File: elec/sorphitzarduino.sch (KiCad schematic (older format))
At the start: 13 parts, among them J1 9V_BATT, J2 SWITCH, J3 AUDIO_JACK, U1 ARDUINO_MICRO_SHIELD

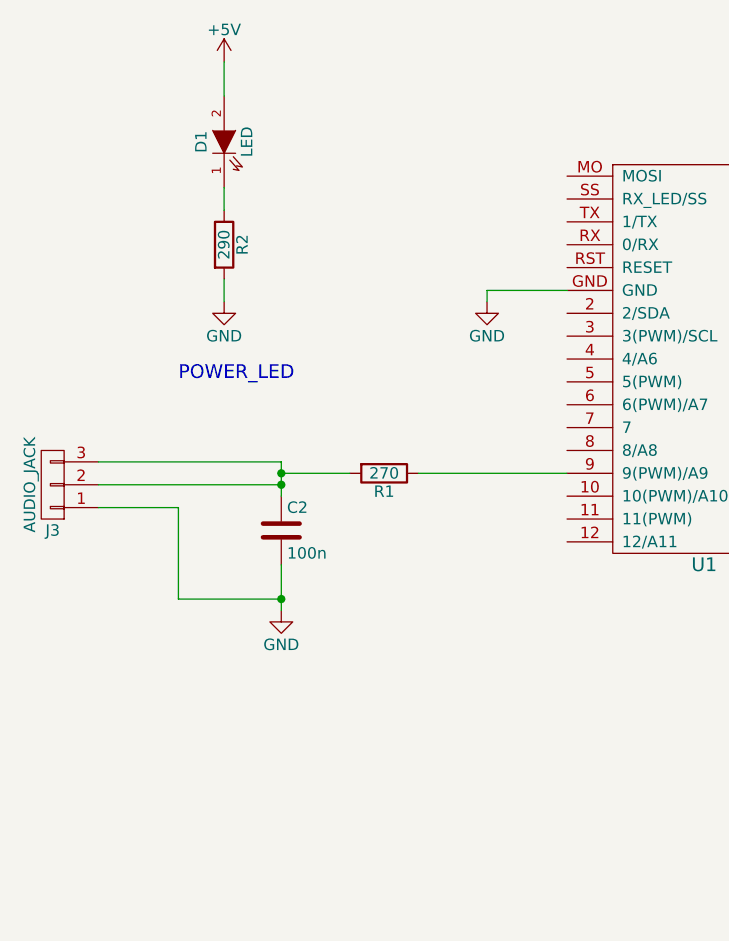
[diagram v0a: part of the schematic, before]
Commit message: Upating to HIFI output circuit, and adding sontrol of LED
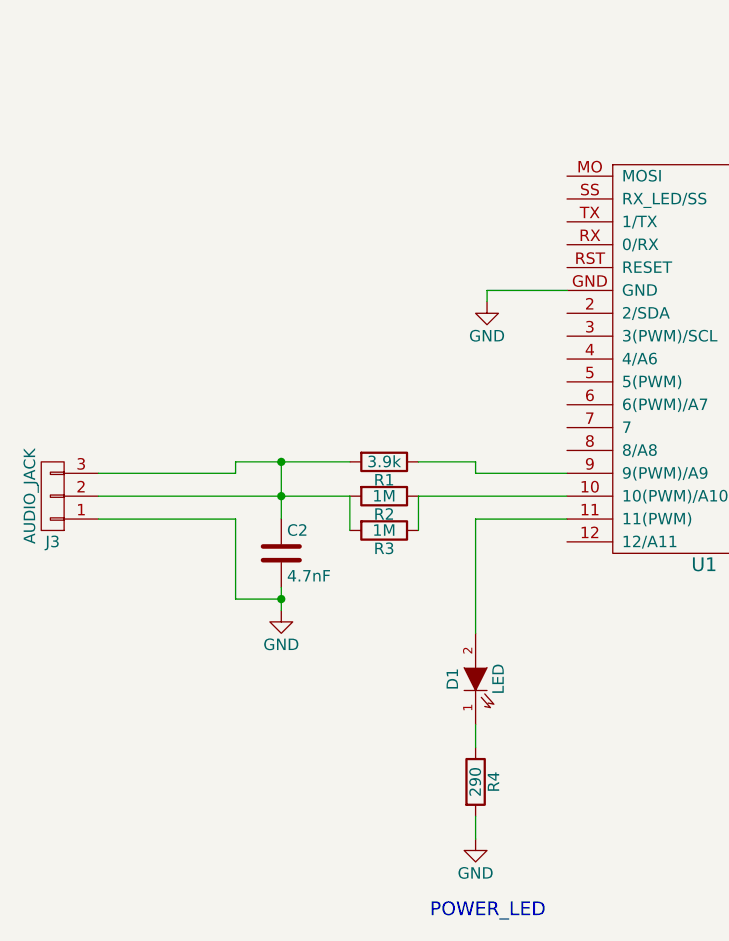
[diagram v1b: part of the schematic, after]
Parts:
- added R2, R3: 1M, Resistors_ThroughHole:Resistor_Horizontal_RM10mm, symbol R
- C2: value 100n -> 4.7nF
- R1: value 270 -> 3.9k
- renumbered R2 to R4
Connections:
- net +5V: no longer D1.2 (A)
- net at U1.10 (10(PWM)/A10): now also R2.1, R3.1
- net at U1.11 (11(PWM)): now also D1.2 (A)
- net at C2.1, J3.2 (P2), J3.3 (P3)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: now also R2.2, R3.2
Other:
- moved on the sheet: C2, D1, J3, R1, R4
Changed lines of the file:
@@
 Connection ~ 7250 3250
-$Comp
-L R R1
-U 1 1 5BFA081C
-P 4500 4250
-F 0 "R1" V 4580 4250 50  0000 C CNN
-F 1 "270" V 4500 4250 50  0000 C CNN
-F 2 "Resistors_ThroughHole:Resistor_Horizontal_RM10mm" V 4430 4250 50  0001 C CNN
-F 3 "" H 4500 4250 50  0000 C CNN
-	1    4500 4250
-	0    1    1    0
-$EndComp
 $Comp
 L C C2
 U 1 1 5BFA0990
-P 4050 4500
-F 0 "C2" H 4075 4600 50  0000 L CNN
-F 1 "100n" H 4075 4400 50  0000 L CNN
-F 2 "Capacitors_ThroughHole:C_Disc_D6_P5" H 4088 4350 50  0001 C CNN
-F 3 "" H 4050 4500 50  0000 C CNN
-	1    4050 4500
+P 4050 4600
+F 0 "C2" H 4075 4700 50  0000 L CNN
+F 1 "4.7nF" H 4075 4500 50  0000 L CNN
+F 2 "Capacitors_ThroughHole:C_Disc_D6_P5" H 4088 4450 50  0001 C CNN
+F 3 "" H 4050 4600 50  0000 C CNN
+	1    4050 4600
 	1    0    0    -1
 $EndComp
@@
 	1    0    0    -1
 $EndComp
-Wire Wire Line
-	4050 4650 4050 4850
-Wire Wire Line
-	4350 4250 4050 4250
-Wire Wire Line
-	4050 4200 4050 4350
-Wire Wire Line
-	4650 4250 5300 4250
 $Comp
 L CONN_01X03 J3
 U 1 1 5BFA0BF7
-P 3050 4300
-F 0 "J3" H 3050 4500 50  0000 C CNN
-F 1 "AUDIO_JACK" V 3150 4300 50  0000 C CNN
-F 2 "Pin_Headers:Pin_Header_Straight_1x03" H 3050 4300 50  0001 C CNN
-F 3 "" H 3050 4300 50  0000 C CNN
-	1    3050 4300
+P 3050 4350
+F 0 "J3" H 3050 4550 50  0000 C CNN
+F 1 "AUDIO_JACK" V 3150 4350 50  0000 C CNN
+F 2 "Pin_Headers:Pin_Header_Straight_1x03" H 3050 4350 50  0001 C CNN
+F 3 "" H 3050 4350 50  0000 C CNN
+	1    3050 4350
 	-1   0    0    1
 $EndComp
 Wire Wire Line
-	3250 4200 4050 4200
-Connection ~ 4050 4250
-Wire Wire Line
-	4050 4300 3250 4300
-Connection ~ 4050 4300
-Wire Wire Line
-	3250 4400 3600 4400
-Wire Wire Line
-	3600 4400 3600 4800
-Wire Wire Line
-	3600 4800 4050 4800
+	3850 4200 4350 4200
+Wire Wire Line
+	3250 4450 3850 4450
+Wire Wire Line
+	3850 4450 3850 4800
+Wire Wire Line
+	3850 4800 4050 4800
 Connection ~ 4050 4800
 $Comp
 L LED D1
 U 1 1 5BFA0F30
-P 3800 2800
-F 0 "D1" H 3800 2900 50  0000 C CNN
-F 1 "LED" H 3800 2700 50  0000 C CNN
-F 2 "LEDs:LED-5MM" H 3800 2800 50  0001 C CNN
-F 3 "" H 3800 2800 50  0000 C CNN
-	1    3800 2800
+P 4900 5150
+F 0 "D1" H 4900 5250 50  0000 C CNN
+F 1 "LED" H 4900 5050 50  0000 C CNN
+F 2 "LEDs:LED-5MM" H 4900 5150 50  0001 C CNN
+F 3 "" H 4900 5150 50  0000 C CNN
+	1    4900 5150
 	0    -1   -1   0
 $EndComp
 $Comp
-L +5V #PWR06
-U 1 1 5BFA10BA
-P 3800 2450
-F 0 "#PWR06" H 3800 2300 50  0001 C CNN
-F 1 "+5V" H 3800 2590 50  0000 C CNN
-F 2 "" H 3800 2450 50  0000 C CNN
-F 3 "" H 3800 2450 50  0000 C CNN
-	1    3800 2450
-	1    0    0    -1
-$EndComp
-$Comp
-L GND #PWR07
+L GND #PWR06
 U 1 1 5BFA10FE
-P 3800 3500
-F 0 "#PWR07" H 3800 3250 50  0001 C CNN
-F 1 "GND" H 3800 3350 50  0000 C CNN
-F 2 "" H 3800 3500 50  0000 C CNN
-F 3 "" H 3800 3500 50  0000 C CNN
-	1    3800 3500
-	1    0    0    -1
-$EndComp
-$Comp
-L R R2
+P 4900 5850
+F 0 "#PWR06" H 4900 5600 50  0001 C CNN
+F 1 "GND" H 4900 5700 50  0000 C CNN
+F 2 "" H 4900 5850 50  0000 C CNN
+F 3 "" H 4900 5850 50  0000 C CNN
+	1    4900 5850
+	1    0    0    -1
+$EndComp
+$Comp
+L R R4
 U 1 1 5BFA11AE
-P 3800 3250
-F 0 "R2" V 3880 3250 50  0000 C CNN
-F 1 "290" V 3800 3250 50  0000 C CNN
-F 2 "Resistors_ThroughHole:Resistor_Horizontal_RM10mm" V 3730 3250 50  0001 C CNN
-F 3 "" H 3800 3250 50  0000 C CNN
-	1    3800 3250
-	1    0    0    -1
-$EndComp
-Wire Wire Line
-	3800 2450 3800 2600
-Wire Wire Line
-	3800 3000 3800 3100
-Wire Wire Line
-	3800 3400 3800 3500
-Text Notes 3600 3850 0    60   ~ 0
+P 4900 5600
+F 0 "R4" V 4980 5600 50  0000 C CNN
+F 1 "290" V 4900 5600 50  0000 C CNN
+F 2 "Resistors_ThroughHole:Resistor_Horizontal_RM10mm" V 4830 5600 50  0001 C CNN
+F 3 "" H 4900 5600 50  0000 C CNN
+	1    4900 5600
+	1    0    0    -1
+$EndComp
+Wire Wire Line
+	4900 5350 4900 5450
+Wire Wire Line
+	4900 5750 4900 5850
+Text Notes 4700 6200 0    60   ~ 0
 POWER_LED
 $Comp
@@
 Connection ~ 7500 4900
 $Comp
-L GND #PWR08
+L GND #PWR07
 U 1 1 5BFA60DB
 P 4950 3500
-F 0 "#PWR08" H 4950 3250 50  0001 C CNN
+F 0 "#PWR07" H 4950 3250 50  0001 C CNN
 F 1 "GND" H 4950 3350 50  0000 C CNN
 F 2 "" H 4950 3500 50  0000 C CNN
@@
 Wire Wire Line
 	4950 3450 4950 3500
+Wire Wire Line
+	5300 4450 4900 4450
+Wire Wire Line
+	4900 4450 4900 4950
+$Comp
+L R R1
+U 1 1 5BFA081C
+P 4500 4200
+F 0 "R1" V 4580 4200 50  0000 C CNN
+F 1 "3.9k" V 4500 4200 50  0000 C CNN
+F 2 "Resistors_ThroughHole:Resistor_Horizontal_RM10mm" V 4430 4200 50  0001 C CNN
+F 3 "" H 4500 4200 50  0000 C CNN
+	1    4500 4200
+	0    1    1    0
+$EndComp
+$Comp
+L R R2
+U 1 1 5C037AD8
+P 4500 4350
+F 0 "R2" V 4580 4350 50  0000 C CNN
+F 1 "1M" V 4500 4350 50  0000 C CNN
+F 2 "Resistors_ThroughHole:Resistor_Horizontal_RM10mm" V 4430 4350 50  0001 C CNN
+F 3 "" H 4500 4350 50  0000 C CNN
+	1    4500 4350
+	0    1    1    0
+$EndComp
+$Comp
+L R R3
+U 1 1 5C037B46
+P 4500 4500
+F 0 "R3" V 4580 4500 50  0000 C CNN
+F 1 "1M" V 4500 4500 50  0000 C CNN
+F 2 "Resistors_ThroughHole:Resistor_Horizontal_RM10mm" V 4430 4500 50  0001 C CNN
+F 3 "" H 4500 4500 50  0000 C CNN
+	1    4500 4500
+	0    1    1    0
+$EndComp
+Wire Wire Line
+	5300 4350 4650 4350
+Wire Wire Line
+	4650 4350 4650 4500
+Wire Wire Line
+	4050 4200 4050 4450
+Wire Wire Line
+	4050 4750 4050 4850
+Wire Wire Line
+	3250 4350 4350 4350
+Wire Wire Line
+	4350 4350 4350 4500
+Wire Wire Line
+	4650 4200 4900 4200
+Wire Wire Line
+	4900 4200 4900 4250
+Wire Wire Line
+	4900 4250 5300 4250
+Connection ~ 4050 4200
+Connection ~ 4050 4350
+Wire Wire Line
+	3250 4250 3850 4250
+Wire Wire Line
+	3850 4250 3850 4200
 $EndSCHEMATC

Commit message: Initial attempts at exporting png files for cutting
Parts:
- C1: symbol CP -> Bourne_PTA6043:CP
- C2: symbol C -> Bourne_PTA6043:C
- D1: symbol LED -> Bourne_PTA6043:LED
- J1, J2: symbol CONN_01X02 -> sorphitzarduino-rescue:CONN_01X02
- J3: symbol CONN_01X03 -> sorphitzarduino-rescue:CONN_01X03
- R1, R2, R3, R4: symbol R -> Bourne_PTA6043:R
- RV1, RV2, RV3, RV4: symbol Bourne_Slider -> Bourne_PTA6043:Bourne_Slider
- U1: symbol ARDUINO_MICRO_SHIELD -> sorphitzarduino-rescue:ARDUINO_MICRO_SHIELD
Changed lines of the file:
@@
-EESchema Schematic File Version 2
-LIBS:power
-LIBS:device
-LIBS:transistors
-LIBS:conn
-LIBS:linear
-LIBS:regul
-LIBS:74xx
-LIBS:cmos4000
-LIBS:adc-dac
-LIBS:memory
-LIBS:xilinx
-LIBS:microcontrollers
-LIBS:dsp
-LIBS:microchip
-LIBS:analog_switches
-LIBS:motorola
-LIBS:texas
-LIBS:intel
-LIBS:audio
-LIBS:interface
-LIBS:digital-audio
-LIBS:philips
-LIBS:display
-LIBS:cypress
-LIBS:siliconi
-LIBS:opto
-LIBS:atmel
-LIBS:contrib
-LIBS:valves
-LIBS:arduino_micro_shield
-LIBS:Bourne_PTA6043
+EESchema Schematic File Version 4
 LIBS:sorphitzarduino-cache
-EELAYER 25 0
+EELAYER 26 0
 EELAYER END
 $Descr A4 11693 8268
@@
 $EndDescr
 $Comp
-L GND #PWR01
+L power:GND #PWR01
 U 1 1 5BF9F106
 P 7100 4950
@@
 $EndComp
 $Comp
-L ARDUINO_MICRO_SHIELD U1
+L sorphitzarduino-rescue:ARDUINO_MICRO_SHIELD U1
 U 1 1 5BF9F1BE
 P 5500 2900
@@
 $EndComp
 $Comp
-L CONN_01X02 J1
+L sorphitzarduino-rescue:CONN_01X02 J1
 U 1 1 5BF9F43C
 P 8150 3200
@@
 $EndComp
 $Comp
-L GND #PWR02
+L power:GND #PWR02
 U 1 1 5BF9F4FC
 P 7100 3350
@@
 $EndComp
 $Comp
-L +5V #PWR03
+L power:+5V #PWR03
 U 1 1 5BF9F94F
 P 6850 4800
@@
 $EndComp
 $Comp
-L +5V #PWR04
+L power:+5V #PWR04
 U 1 1 5BF9F98F
 P 6850 3450
@@
 	7950 3150 7550 3150
 Wire Wire Line
-	7050 2800 7400 2800
-Wire Wire Line
-	6650 3250 7950 3250
+	7050 2800 7250 2800
+Wire Wire Line
+	6650 3250 7100 3250
 Wire Wire Line
 	7100 3350 7100 3250
@@
 	6850 4800 7050 4800
 $Comp
-L CONN_01X02 J2
+L sorphitzarduino-rescue:CONN_01X02 J2
 U 1 1 5BF9FCCD
 P 8150 2550
@@
 Wire Wire Line
 	7550 2600 7550 3150
-Connection ~ 7550 3150
 Wire Wire Line
 	7950 2500 7400 2500
 Wire Wire Line
 	7400 2500 7400 2800
-Connection ~ 7400 2800
-Wire Wire Line
-	7050 4350 7050 4900
+Wire Wire Line
+	7050 4350 7050 4800
 Wire Wire Line
 	7050 4350 6650 4350
@@
 	7050 3150 6650 3150
 $Comp
-L CP C1
+L Bourne_PTA6043:CP C1
 U 1 1 5BFA0508
 P 7250 3000
@@
 Connection ~ 7250 3250
 $Comp
-L C C2
+L Bourne_PTA6043:C C2
 U 1 1 5BFA0990
 P 4050 4600
@@
 $EndComp
 $Comp
-L GND #PWR05
+L power:GND #PWR05
 U 1 1 5BFA09E9
 P 4050 4850
@@
 $EndComp
 $Comp
-L CONN_01X03 J3
+L sorphitzarduino-rescue:CONN_01X03 J3
 U 1 1 5BFA0BF7
 P 3050 4350
@@
 $EndComp
 Wire Wire Line
-	3850 4200 4350 4200
+	3850 4200 4050 4200
 Wire Wire Line
 	3250 4450 3850 4450
@@
 Connection ~ 4050 4800
 $Comp
-L LED D1
+L Bourne_PTA6043:LED D1
 U 1 1 5BFA0F30
 P 4900 5150
@@
 $EndComp
 $Comp
-L GND #PWR06
+L power:GND #PWR06
 U 1 1 5BFA10FE
 P 4900 5850
@@
 $EndComp
 $Comp
-L R R4
+L Bourne_PTA6043:R R4
 U 1 1 5BFA11AE
 P 4900 5600
@@
 POWER_LED
 $Comp
-L Bourne_Slider RV1
+L Bourne_PTA6043:Bourne_Slider RV1
 U 1 1 5BFA5669
 P 7750 4600
@@
 $EndComp
 $Comp
-L Bourne_Slider RV2
+L Bourne_PTA6043:Bourne_Slider RV2
 U 1 1 5BFA57ED
 P 8450 4600
@@
 $EndComp
 $Comp
-L Bourne_Slider RV3
+L Bourne_PTA6043:Bourne_Slider RV3
 U 1 1 5BFA5836
 P 9150 4600
@@
 $EndComp
 $Comp
-L Bourne_Slider RV4
+L Bourne_PTA6043:Bourne_Slider RV4
 U 1 1 5BFA58DD
 P 9850 4600
@@
 	9850 3950 6650 3950
 Wire Wire Line
-	7100 4950 10100 4950
+	7100 4950 8000 4950
 Wire Wire Line
 	10100 4950 10100 4600
@@
 Connection ~ 8000 4950
 Wire Wire Line
-	7050 4900 9600 4900
+	7050 4900 7500 4900
 Wire Wire Line
 	9600 4900 9600 4600
@@
 Connection ~ 7500 4900
 $Comp
-L GND #PWR07
+L power:GND #PWR07
 U 1 1 5BFA60DB
 P 4950 3500
@@
 	4900 4450 4900 4950
 $Comp
-L R R1
+L Bourne_PTA6043:R R1
 U 1 1 5BFA081C
 P 4500 4200
@@
 $EndComp
 $Comp
-L R R2
+L Bourne_PTA6043:R R2
 U 1 1 5C037AD8
 P 4500 4350
@@
 $EndComp
 $Comp
-L R R3
+L Bourne_PTA6043:R R3
 U 1 1 5C037B46
 P 4500 4500
@@
 	4650 4350 4650 4500
 Wire Wire Line
-	4050 4200 4050 4450
-Wire Wire Line
-	4050 4750 4050 4850
-Wire Wire Line
-	3250 4350 4350 4350
+	4050 4200 4050 4350
+Wire Wire Line
+	4050 4750 4050 4800
+Wire Wire Line
+	3250 4350 4050 4350
 Wire Wire Line
 	4350 4350 4350 4500
@@
 Wire Wire Line
 	3850 4250 3850 4200
+Wire Wire Line
+	7100 3250 7250 3250
+Wire Wire Line
+	7050 4800 7050 4900
+Wire Wire Line
+	7250 2800 7400 2800
+Wire Wire Line
+	7250 3250 7950 3250
+Wire Wire Line
+	4050 4800 4050 4850
+Wire Wire Line
+	9400 4950 10100 4950
+Wire Wire Line
+	8700 4950 9400 4950
+Wire Wire Line
+	8000 4950 8700 4950
+Wire Wire Line
+	8900 4900 9600 4900
+Wire Wire Line
+	8200 4900 8900 4900
+Wire Wire Line
+	7500 4900 8200 4900
+Wire Wire Line
+	4050 4200 4350 4200
+Wire Wire Line
+	4050 4350 4050 4450
+Wire Wire Line
+	4050 4350 4350 4350
 $EndSCHEMATC

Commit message: Generating better PNG files for milling
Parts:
- added J4, J? (x3): Mounting Hole, MountingHole:MountingHole_3.2mm_M3, symbol Connector_Generic:Conn_01x01
- C1: symbol Bourne_PTA6043:CP -> sorphitzarduino-rescue:CP-Bourne_PTA6043
- C2: symbol Bourne_PTA6043:C -> sorphitzarduino-rescue:C-Bourne_PTA6043
- D1: symbol Bourne_PTA6043:LED -> sorphitzarduino-rescue:LED-Bourne_PTA6043
- J1, J2: symbol sorphitzarduino-rescue:CONN_01X02 -> sorphitzarduino-rescue:CONN_01X02-sorphitzarduino-rescue
- J3: symbol sorphitzarduino-rescue:CONN_01X03 -> sorphitzarduino-rescue:CONN_01X03-sorphitzarduino-rescue
- R1, R2, R3, R4: symbol Bourne_PTA6043:R -> sorphitzarduino-rescue:R-Bourne_PTA6043
- RV1, RV2, RV3, RV4: symbol Bourne_PTA6043:Bourne_Slider -> sorphitzarduino-rescue:Bourne_Slider-Bourne_PTA6043
- U1: symbol sorphitzarduino-rescue:ARDUINO_MICRO_SHIELD -> sorphitzarduino-rescue:ARDUINO_MICRO_SHIELD-sorphitzarduino-rescue
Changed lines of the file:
@@
 $EndComp
 $Comp
-L sorphitzarduino-rescue:ARDUINO_MICRO_SHIELD U1
+L sorphitzarduino-rescue:ARDUINO_MICRO_SHIELD-sorphitzarduino-rescue U1
 U 1 1 5BF9F1BE
 P 5500 2900
@@
 $EndComp
 $Comp
-L sorphitzarduino-rescue:CONN_01X02 J1
+L sorphitzarduino-rescue:CONN_01X02-sorphitzarduino-rescue J1
 U 1 1 5BF9F43C
 P 8150 3200
@@
 	6850 4800 7050 4800
 $Comp
-L sorphitzarduino-rescue:CONN_01X02 J2
+L sorphitzarduino-rescue:CONN_01X02-sorphitzarduino-rescue J2
 U 1 1 5BF9FCCD
 P 8150 2550
@@
 	7050 3150 6650 3150
 $Comp
-L Bourne_PTA6043:CP C1
+L sorphitzarduino-rescue:CP-Bourne_PTA6043 C1
 U 1 1 5BFA0508
 P 7250 3000
@@
 Connection ~ 7250 3250
 $Comp
-L Bourne_PTA6043:C C2
+L sorphitzarduino-rescue:C-Bourne_PTA6043 C2
 U 1 1 5BFA0990
 P 4050 4600
@@
 $EndComp
 $Comp
-L sorphitzarduino-rescue:CONN_01X03 J3
+L sorphitzarduino-rescue:CONN_01X03-sorphitzarduino-rescue J3
 U 1 1 5BFA0BF7
 P 3050 4350
@@
 Connection ~ 4050 4800
 $Comp
-L Bourne_PTA6043:LED D1
+L sorphitzarduino-rescue:LED-Bourne_PTA6043 D1
 U 1 1 5BFA0F30
 P 4900 5150
@@
 $EndComp
 $Comp
-L Bourne_PTA6043:R R4
+L sorphitzarduino-rescue:R-Bourne_PTA6043 R4
 U 1 1 5BFA11AE
 P 4900 5600
@@
 POWER_LED
 $Comp
-L Bourne_PTA6043:Bourne_Slider RV1
+L sorphitzarduino-rescue:Bourne_Slider-Bourne_PTA6043 RV1
 U 1 1 5BFA5669
 P 7750 4600
@@
 $EndComp
 $Comp
-L Bourne_PTA6043:Bourne_Slider RV2
+L sorphitzarduino-rescue:Bourne_Slider-Bourne_PTA6043 RV2
 U 1 1 5BFA57ED
 P 8450 4600
@@
 $EndComp
 $Comp
-L Bourne_PTA6043:Bourne_Slider RV3
+L sorphitzarduino-rescue:Bourne_Slider-Bourne_PTA6043 RV3
 U 1 1 5BFA5836
 P 9150 4600
@@
 $EndComp
 $Comp
-L Bourne_PTA6043:Bourne_Slider RV4
+L sorphitzarduino-rescue:Bourne_Slider-Bourne_PTA6043 RV4
 U 1 1 5BFA58DD
 P 9850 4600
@@
 	4900 4450 4900 4950
 $Comp
-L Bourne_PTA6043:R R1
+L sorphitzarduino-rescue:R-Bourne_PTA6043 R1
 U 1 1 5BFA081C
 P 4500 4200
@@
 $EndComp
 $Comp
-L Bourne_PTA6043:R R2
+L sorphitzarduino-rescue:R-Bourne_PTA6043 R2
 U 1 1 5C037AD8
 P 4500 4350
@@
 $EndComp
 $Comp
-L Bourne_PTA6043:R R3
+L sorphitzarduino-rescue:R-Bourne_PTA6043 R3
 U 1 1 5C037B46
 P 4500 4500
@@
 Wire Wire Line
 	4050 4350 4350 4350
+$Comp
+L Connector_Generic:Conn_01x01 J4
+U 1 1 5C079185
+P 3000 2000
+F 0 "J4" H 3079 2042 50  0000 L CNN
+F 1 "Mounting Hole" H 3079 1951 50  0000 L CNN
+F 2 "MountingHole:MountingHole_3.2mm_M3" H 3000 2000 50  0001 C CNN
+F 3 "~" H 3000 2000 50  0001 C CNN
+	1    3000 2000
+	1    0    0    -1
+$EndComp
+$Comp
+L Connector_Generic:Conn_01x01 J?
+U 1 1 5C07ACAF
+P 3000 2250
+F 0 "J?" H 3079 2292 50  0000 L CNN
+F 1 "Mounting Hole" H 3079 2201 50  0000 L CNN
+F 2 "MountingHole:MountingHole_3.2mm_M3" H 3000 2250 50  0001 C CNN
+F 3 "~" H 3000 2250 50  0001 C CNN
+	1    3000 2250
+	1    0    0    -1
+$EndComp
+$Comp
+L Connector_Generic:Conn_01x01 J?
+U 1 1 5C07AD05
+P 3000 2450
+F 0 "J?" H 3079 2492 50  0000 L CNN
+F 1 "Mounting Hole" H 3079 2401 50  0000 L CNN
+F 2 "MountingHole:MountingHole_3.2mm_M3" H 3000 2450 50  0001 C CNN
+F 3 "~" H 3000 2450 50  0001 C CNN
+	1    3000 2450
+	1    0    0    -1
+$EndComp
+$Comp
+L Connector_Generic:Conn_01x01 J?
+U 1 1 5C07AD41
+P 3000 2650
+F 0 "J?" H 3079 2692 50  0000 L CNN
+F 1 "Mounting Hole" H 3079 2601 50  0000 L CNN
+F 2 "MountingHole:MountingHole_3.2mm_M3" H 3000 2650 50  0001 C CNN
+F 3 "~" H 3000 2650 50  0001 C CNN
+	1    3000 2650
+	1    0    0    -1
+$EndComp
 $EndSCHEMATC
